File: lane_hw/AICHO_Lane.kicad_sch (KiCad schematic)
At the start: 65 parts, among them J1 JST PH, J2 RJ45, J41 JST PH, J42 JST PH, J43 JST PH, J9 Conn_01x04, Q41 AO3400A, Q42 AO3400A, Q43 AO3400A, U1 TPS54302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

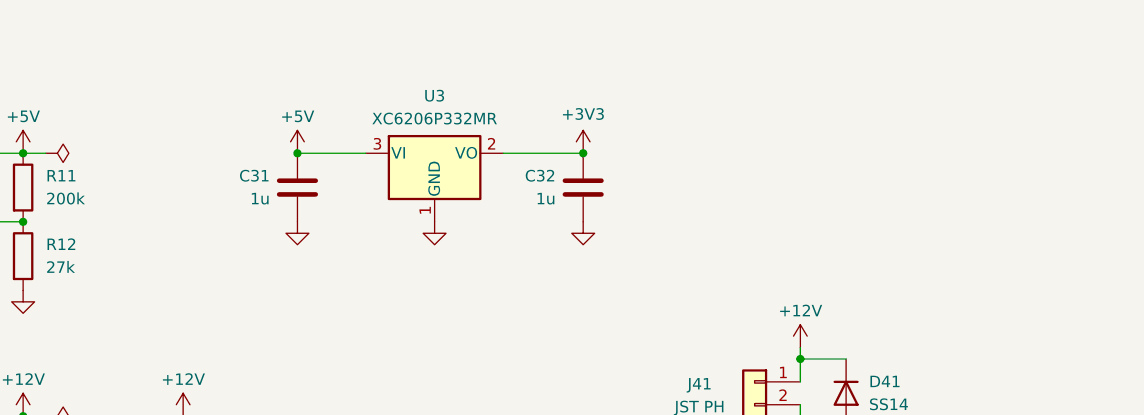
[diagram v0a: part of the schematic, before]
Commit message: lane_hw: Add bulk capacitors and mounting holes
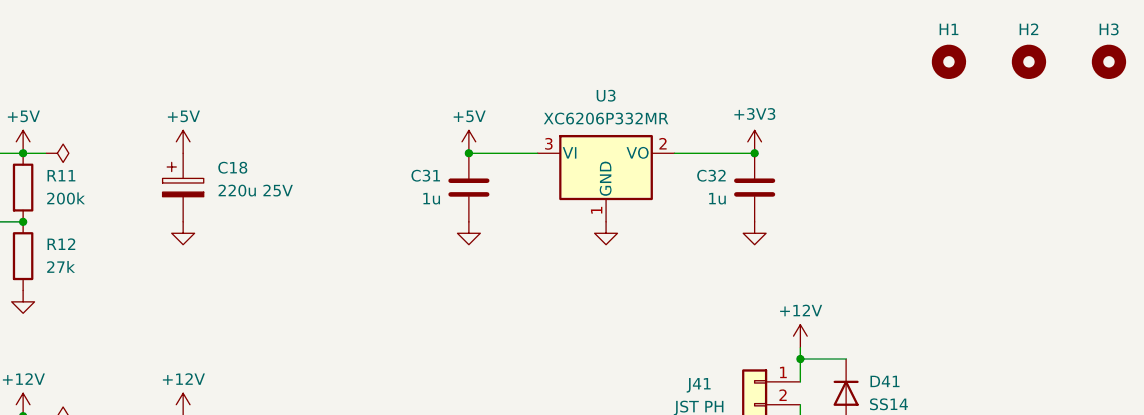
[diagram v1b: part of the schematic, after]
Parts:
- added C18: 220u 25V, Capacitor_SMD:CP_Elec_6.3x7.7, symbol Device:C_Polarized
- added H1, H2, H3: MountingHole, MountingHole:MountingHole_2.2mm_M2, symbol Mechanical:MountingHole
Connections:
- net +5V: now also C18.1
- net GND: now also C18.2
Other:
- moved on the sheet: C31, C32, U3

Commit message: lane_hw: Modify attributes per fabrication settings
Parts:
- J1: LCSC PN (none) -> C7433649
- J41, J42, J43: LCSC PN C51940124 -> C7433648
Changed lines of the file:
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@@
 			)
 		)
-		(property "LCSC PN" "C51940124"
+		(property "LCSC PN" "C7433648"
 			(at 232.41 57.15 0)
 			(effects
@@
 			)
 		)
+		(property "LCSC PN" "C7433649"
+			(at 33.02 102.87 0)
+			(effects
+				(font
+					(size 1.27 1.27)
+				)
+				(hide yes)
+			)
+		)
 		(pin "MP"
 		)
@@
 			)
 		)
-		(property "LCSC PN" "C51940124"
+		(property "LCSC PN" "C7433648"
 			(at 232.41 96.52 0)
 			(effects
@@
 			)
 		)
-		(property "LCSC PN" "C51940124"
+		(property "LCSC PN" "C7433648"
 			(at 232.41 135.89 0)
 			(effects
